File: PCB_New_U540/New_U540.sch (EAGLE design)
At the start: 82 parts, among them IC1 TXB0108PWR, IC2 TXB0108PWR, IC3 TPS76201DBVR, IC4 TPS76201DBVR, IC5 TPS76201DBVR, J4 2985-6004, J5 2985-6004, Q1 BSH103,235, Q2 BSH103,235, Q3 BSH103,235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

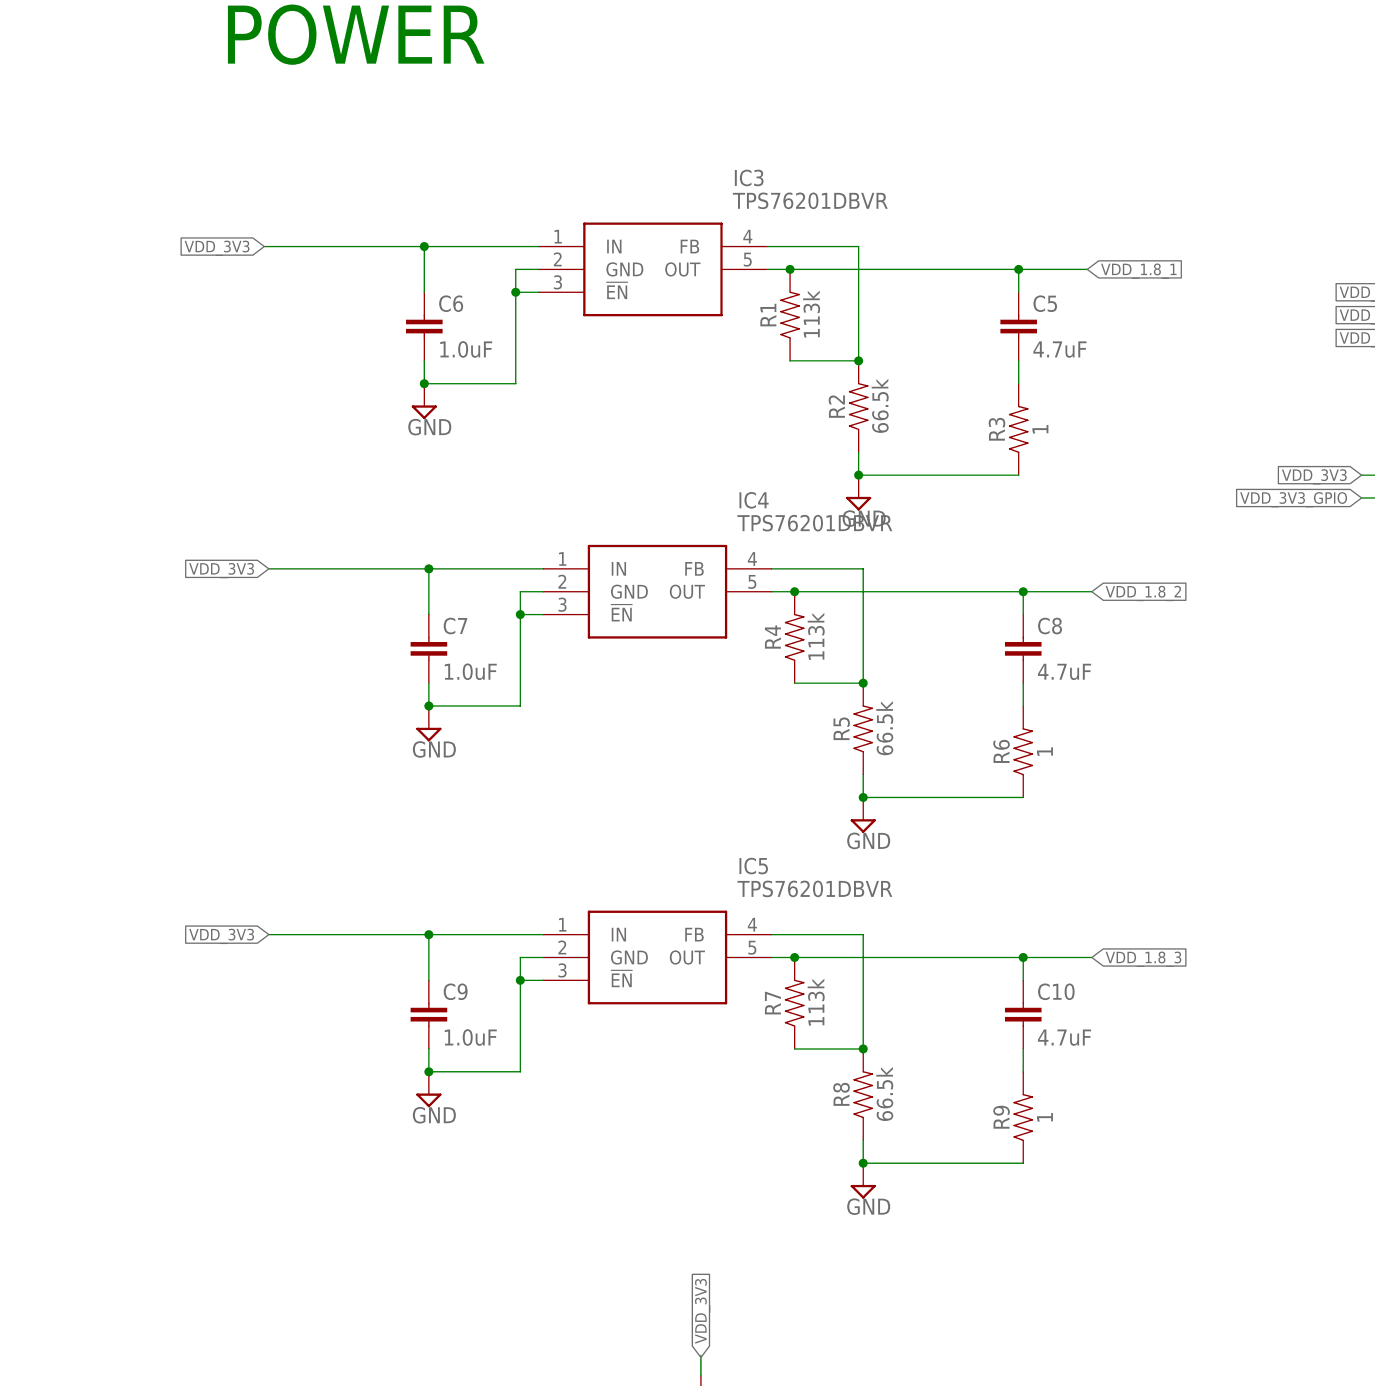
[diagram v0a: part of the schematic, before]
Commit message: Change regulators for higher current
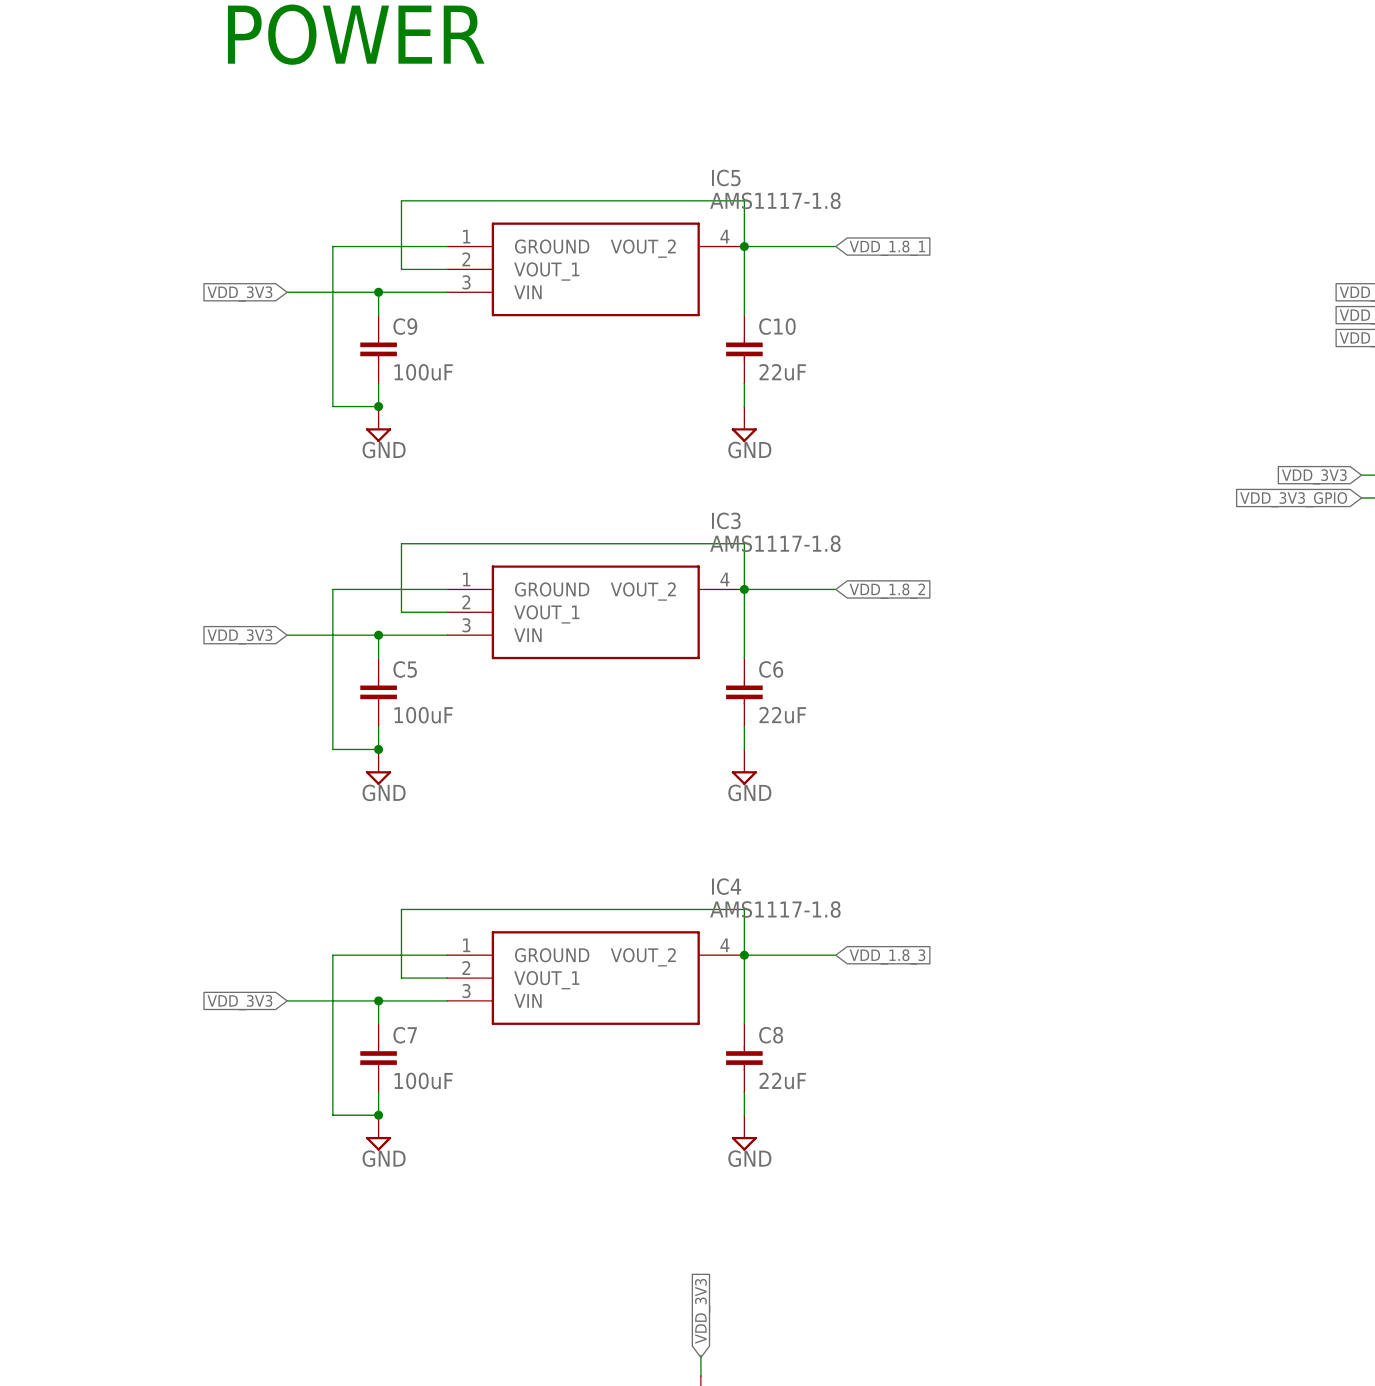
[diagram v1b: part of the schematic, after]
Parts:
- removed R1, R4, R7: 113k, SparkFun-Resistors:RESISTOR1206
- removed R2, R5, R8: 66.5k, SparkFun-Resistors:RESISTOR1206
- removed R3, R6, R9: 1, SparkFun-Resistors:RESISTOR1206
- C10, C8: value 4.7uF -> 22uF
- C5: value 4.7uF -> 100uF
- C6: value 1.0uF -> 22uF
- C7, C9: value 1.0uF -> 100uF
- IC3, IC4, IC5: value TPS76201DBVR -> AMS1117-1.8; device SamacSys_Parts:TPS76201DBVR -> SamacSys_Parts:AMS1117
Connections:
- removed net N$16: IC3.FB, R1.1, R2.2
- removed net N$17: C5.2, R3.2
- removed net N$18: IC4.FB, R4.1, R5.2
- removed net N$19: C8.2, R6.2
- removed net N$20: IC5.FB, R7.1, R8.2
- removed net N$21: C10.2, R9.2
- net GND: now also C10.2, C5.2, C8.2, IC3.GROUND, IC4.GROUND, IC5.GROUND; no longer IC3.!EN, IC3.GND, IC4.!EN, IC4.GND, IC5.!EN, IC5.GND, R2.1, R3.1, R5.1, R6.1, R8.1, R9.1
- net VDD_1.8_1: now also C10.1, IC5.VOUT_1, IC5.VOUT_2; no longer C5.1, IC3.OUT, R1.2
- net VDD_1.8_2: now also C6.1, IC3.VOUT_1, IC3.VOUT_2; no longer C8.1, IC4.OUT, R4.2
- net VDD_1.8_3: now also C8.1, IC4.VOUT_1, IC4.VOUT_2; no longer C10.1, IC5.OUT, R7.2
- net VDD_3V3: now also C5.1, IC3.VIN, IC4.VIN, IC5.VIN; no longer C6.1, IC3.IN, IC4.IN, IC5.IN
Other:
- moved on the sheet: C10, C5, C6, C7, C8, C9
